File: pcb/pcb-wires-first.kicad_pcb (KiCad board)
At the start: 2 copper layers, 55 x 70 mm, 42 parts, among them J4 Conn_01x02, J5 Conn_01x02, J6 Conn_01x04, J8 Conn_01x04, SW7 set, SW8 reset, SW9 toggle, U2 SLG47115V, U3 R-78C3.3-1.0

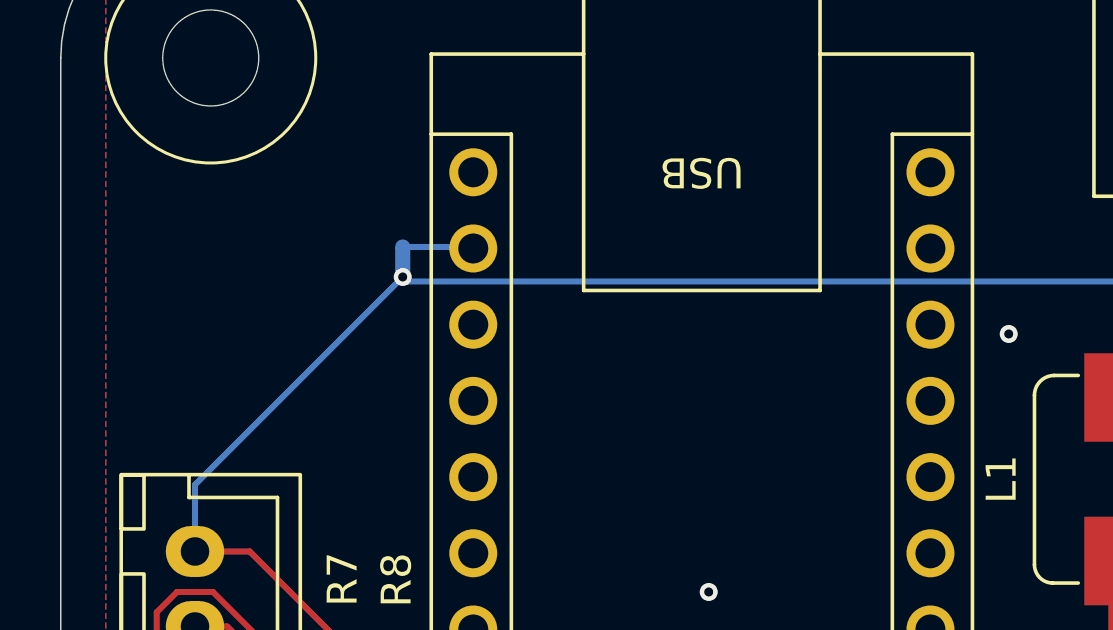
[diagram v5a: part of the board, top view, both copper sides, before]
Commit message: Adding blinker for Arduino.
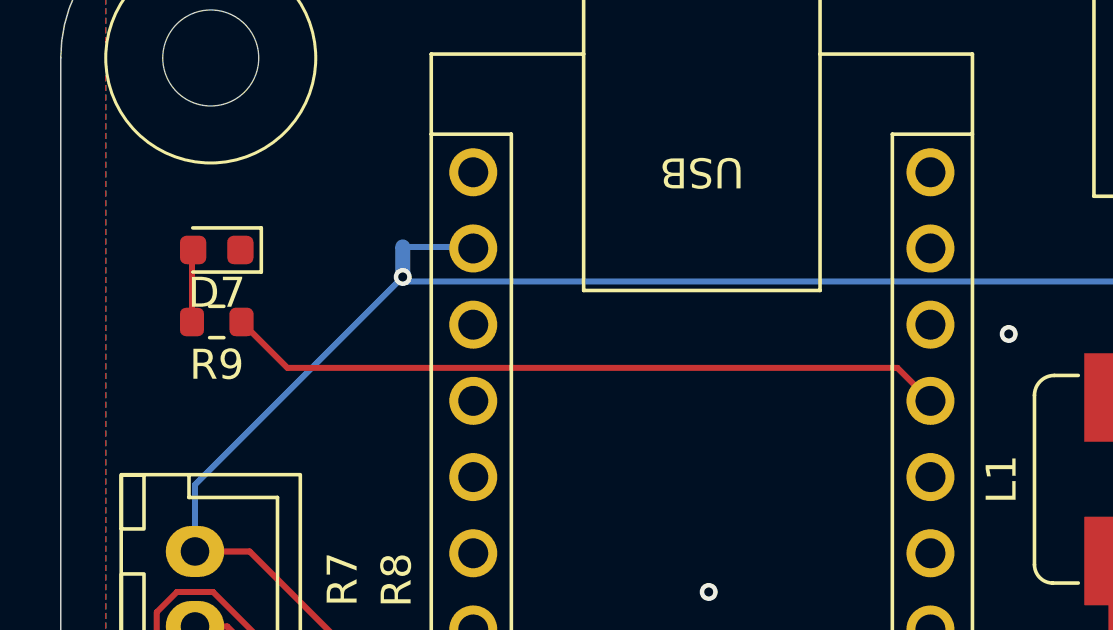
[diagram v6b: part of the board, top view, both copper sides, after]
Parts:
- added D7: 3V3, Diode_SMD:D_0603_1608Metric, F.Cu at (65.2, 86.4)
- added R9: 2.2k, Resistor_SMD:R_0603_1608Metric, F.Cu at (65.2, 88.8)
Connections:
- A1 pad 12: unconnected-(A1-D9-Pad12) -> Net-(A1-D9)
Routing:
- net Net-(A1-D9): track 0.00 -> 24.1 mm
- net Net-(D7-A): track 0.00 -> 2.42 mm

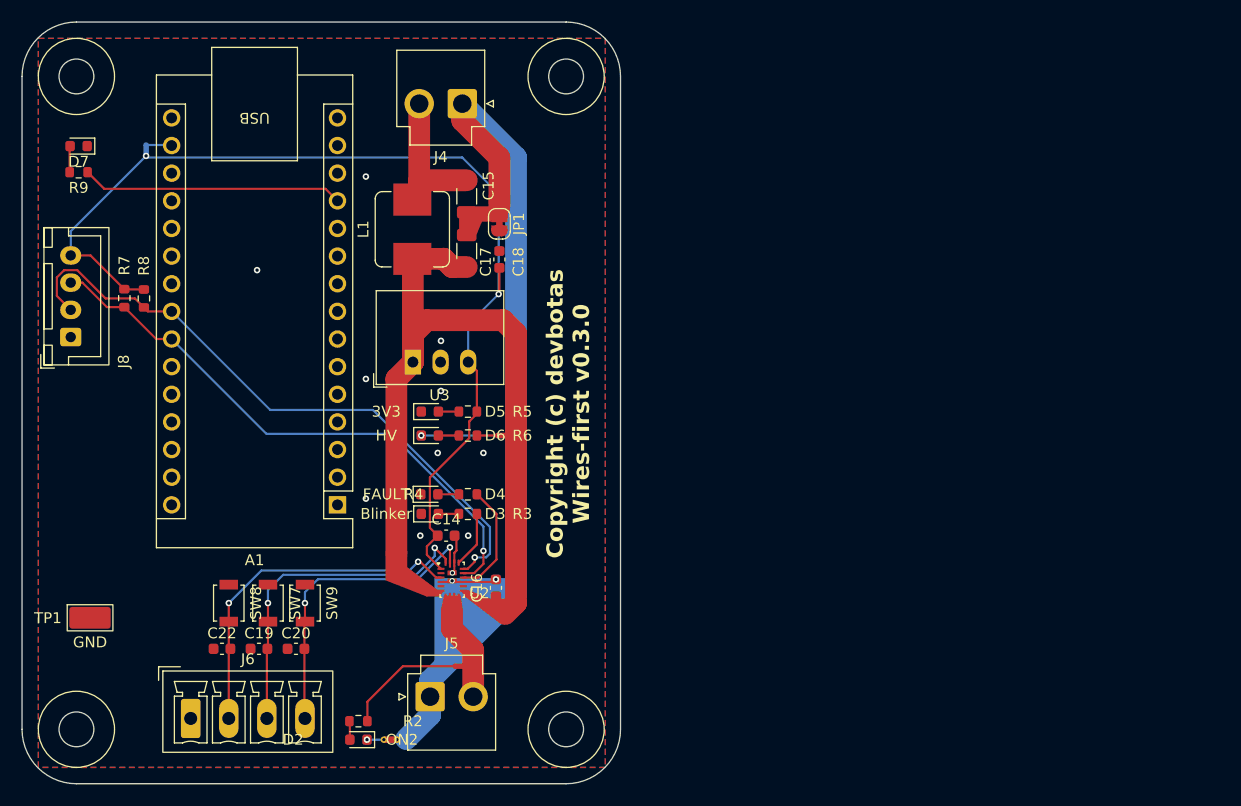
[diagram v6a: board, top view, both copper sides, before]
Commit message: Cleaning up DRC violations in PCB.
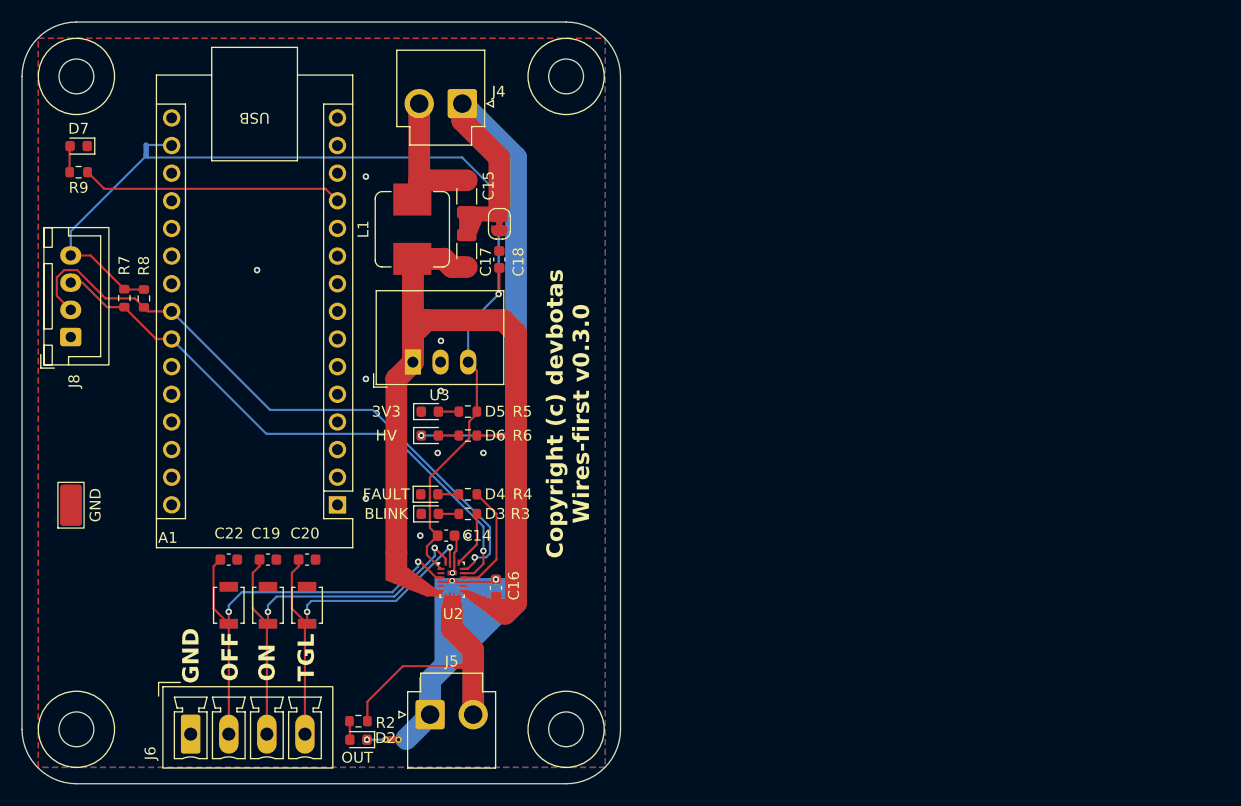
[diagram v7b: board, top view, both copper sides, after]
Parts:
- D2: value ON2 -> OUT
- D3: value Blinker -> BLINK
- J8: value Conn_01x04 -> I2C
- moved TP1 10.5 mm to (64.5, 119.4), turned to 90 degrees
- moved C20 8.26 mm to (86.2, 124.4), turned to 180 degrees
- moved C19 8.24 mm to (82.6, 124.4), turned to 180 degrees
- moved C22 8.22 mm to (79.0, 124.4), turned to 180 degrees
- moved J5 1.65 mm to (97.5, 138.7)
- moved J6 1.44 mm to (75.5, 140.4)
- moved SW9 0.28 mm to (86.2, 128.6)
- moved SW7 0.20 mm to (82.6, 128.6)
- moved SW8 0.20 mm to (79.0, 128.6)
- moved NT5 0.15 mm to (94.6, 140.9)
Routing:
- net Net-(J6-Pin_2): track 32.4 -> 40.6 mm
- net Net-(J6-Pin_4): track 28.2 -> 35.6 mm
- net Net-(J6-Pin_3): track 31.0 -> 38.4 mm
- net /output: track 8.56 -> 10.2 mm
- net 3V3: vias 2 -> 1
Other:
- board text added: "GND"
- board text added: "OFF"
- board text added: "ON"
- board text added: "TGL"

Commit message: Some more cleanup.
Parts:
- moved R7 7.06 mm to (71.2, 107.2), turned to 90 degrees
- moved R8 7.01 mm to (69.4, 107.2), turned to 90 degrees
- moved J4 1.46 mm to (101.4, 81.3)
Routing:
- net 3V3: track 95.5 -> 106.4 mm
- net SCL: track 52.8 -> 59.3 mm
- net HV-GND: track 75.5 -> 77.1 mm
- net /hv-in-1: track 13.5 -> 14.9 mm
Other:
- board text added: "3V3"
- board text added: "OUT"
- board text added: "PWR IN 12-24V"
- board text added: "SCL"
- board text added: "SDA"
